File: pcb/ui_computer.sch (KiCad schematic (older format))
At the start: 0 parts

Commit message: updated power, caps, io
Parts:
- added C?: 0.1uF, RespiraWorks_Std:C_0603_1608Metric, symbol Device:C
- added C?: 1uF, RespiraWorks_Std:C_0603_1608Metric, symbol Device:C
- added H?: RaspberryPi, RespiraWorks:RaspberryPi, symbol RespiraWorks:RaspberryPi
- added J?: ESQ-120-44-L-D, RespiraWorks_Std:PinHeader_2x20_P2.54mm_Vertical, symbol RespiraWorks:ESQ-120-44-L-D
- added R? (x2): 10K, RespiraWorks_std:R_0603_1608Metric, symbol Device:R
- added R? (x2): 1K, RespiraWorks_std:R_0603_1608Metric, symbol Device:R
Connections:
- new net +3V3_Rpi: J?.1 (3V3_power), J?.17 (3V3_power), R?.1, R?.1
- new net 5V_GUI: C?.1, C?.1, J?.2 (5V_power), J?.4 (5V_power)
- new net GND: C?.2, C?.2, H?.1, J?.14 (GND), J?.20 (GND), J?.25 (GND), J?.30 (GND), J?.34 (GND), J?.39 (GND), J?.6 (GND), J?.9 (GND), R?.2, R?.2
- new net GPIO0(ID_SD): J?.27 (GPIO0(ID_SD))
- new net GPIO1(ID_SC): J?.28 (GPIO1(ID_SC))
- new net GPIO10(MOSI): J?.19 (GPIO10(MOSI))
- new net GPIO11(SCLK): J?.23 (GPIO11(SCLK))
- new net GPIO12(PWM0): J?.32 (GPIO12(PWM0))
- new net GPIO13(PWM1): J?.33 (GPIO13(PWM1))
- new net GPIO14(TXD): J?.8 (GPIO14(TXD))
- new net GPIO15(RXD): J?.10 (GPIO15(RXD))
- new net GPIO16: J?.36 (GPIO16)
- new net GPIO17: J?.11 (GPIO17)
- new net GPIO18(PCM_CLK): J?.12 (GPIO18(PCM_CLK))
- new net GPIO19(PCM_FS): J?.35 (GPIO19(PCM_FS))
- new net GPIO2(SDA): J?.3 (GPIO2(SDA))
- new net GPIO20(PCM_DIN): J?.38 (GPIO20(PCM_DIN))
- new net GPIO21(PCM_DOUT): J?.40 (GPIO21(PCM_DOUT))
- new net GPIO22: J?.15 (GPIO22)
- new net GPIO23: J?.16 (GPIO23)
- new net GPIO24: J?.18 (GPIO24)
- new net GPIO27: J?.13 (GPIO27)
- new net GPIO3(SCL): J?.5 (GPIO3(SCL))
- new net GPIO4(GPCLK0): J?.7 (GPIO4(GPCLK0))
- new net GPIO5: J?.29 (GPIO5)
- new net GPIO6: J?.31 (GPIO6)
- new net GPIO7(CE1): J?.26 (GPIO7(CE1))
- new net GPIO8(CE0): J?.24 (GPIO8(CE0))
- new net GPIO9(MISO): J?.21 (GPIO9(MISO))
- new net UI_ID0: J?.22 (GPIO25), R?.1, R?.2
- new net UI_ID1: J?.37 (GPIO26), R?.1, R?.2
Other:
- note added: "RPI powered by 5V\n"
- note added: "USB TO UART adapter: https://www.ftdichip.com/Support/Documents/DataSheets/Modules/DS_DB9-USB-RS232.pdf"

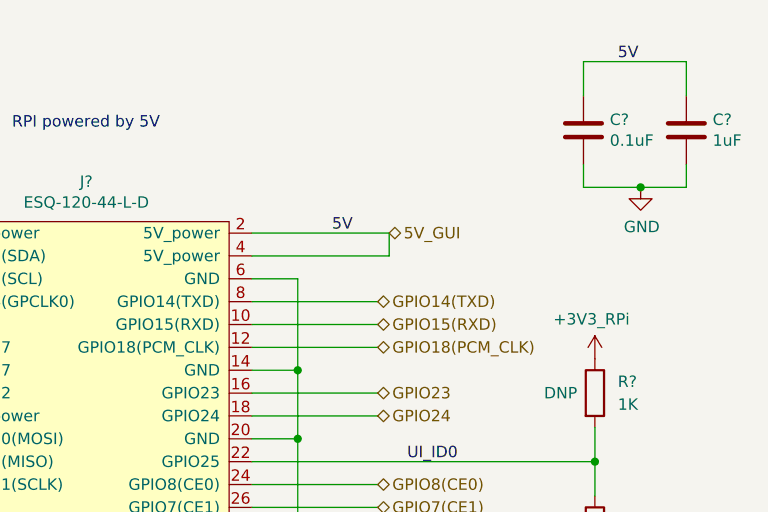
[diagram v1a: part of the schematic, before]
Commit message: Top-level beginnings, minor fixes
Started on top-level schematic blocks and connections
Started changing some net names to mixed-case-with-dash format
Fixed version number, added titles and version to all schematic sheets
Fixed incorrect SWO pin assignment in cycle controller
Added a few add'l annotations to battery sheets
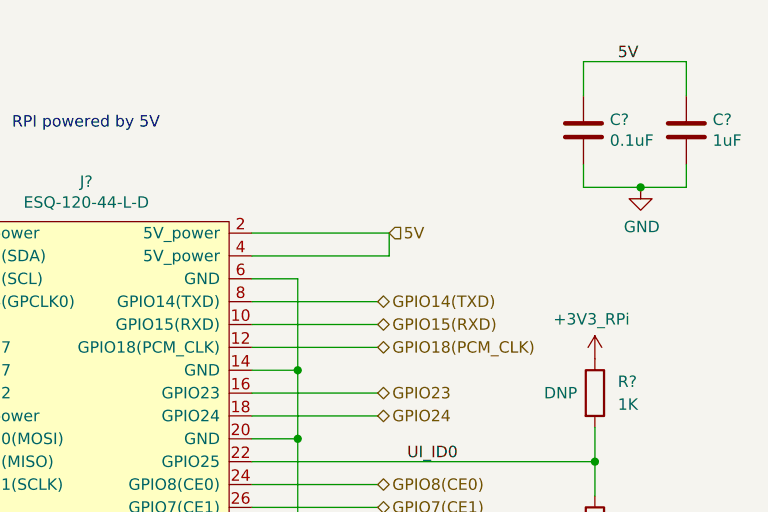
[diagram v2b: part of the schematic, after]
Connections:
- net 5V_GUI renamed 5V
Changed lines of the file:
@@
 EESchema Schematic File Version 4
-LIBS:ui_computer-cache
-EELAYER 26 0
+EELAYER 30 0
 EELAYER END
 $Descr A4 11693 8268
 encoding utf-8
-Sheet 1 1
+Sheet 8 37
 Title "UI Computer"
 Date ""
-Rev "2.0"
+Rev "A"
 Comp "RespiraWorks"
 Comment1 ""
@@
 Wire Wire Line
 	6450 4200 7000 4200
-Text HLabel 7050 2300 2    50   BiDi ~ 0
-5V_GUI
-Text Label 6800 2300 0    50   ~ 0
+Text HLabel 7050 2300 2    50   Input ~ 0
 5V
 Wire Wire Line

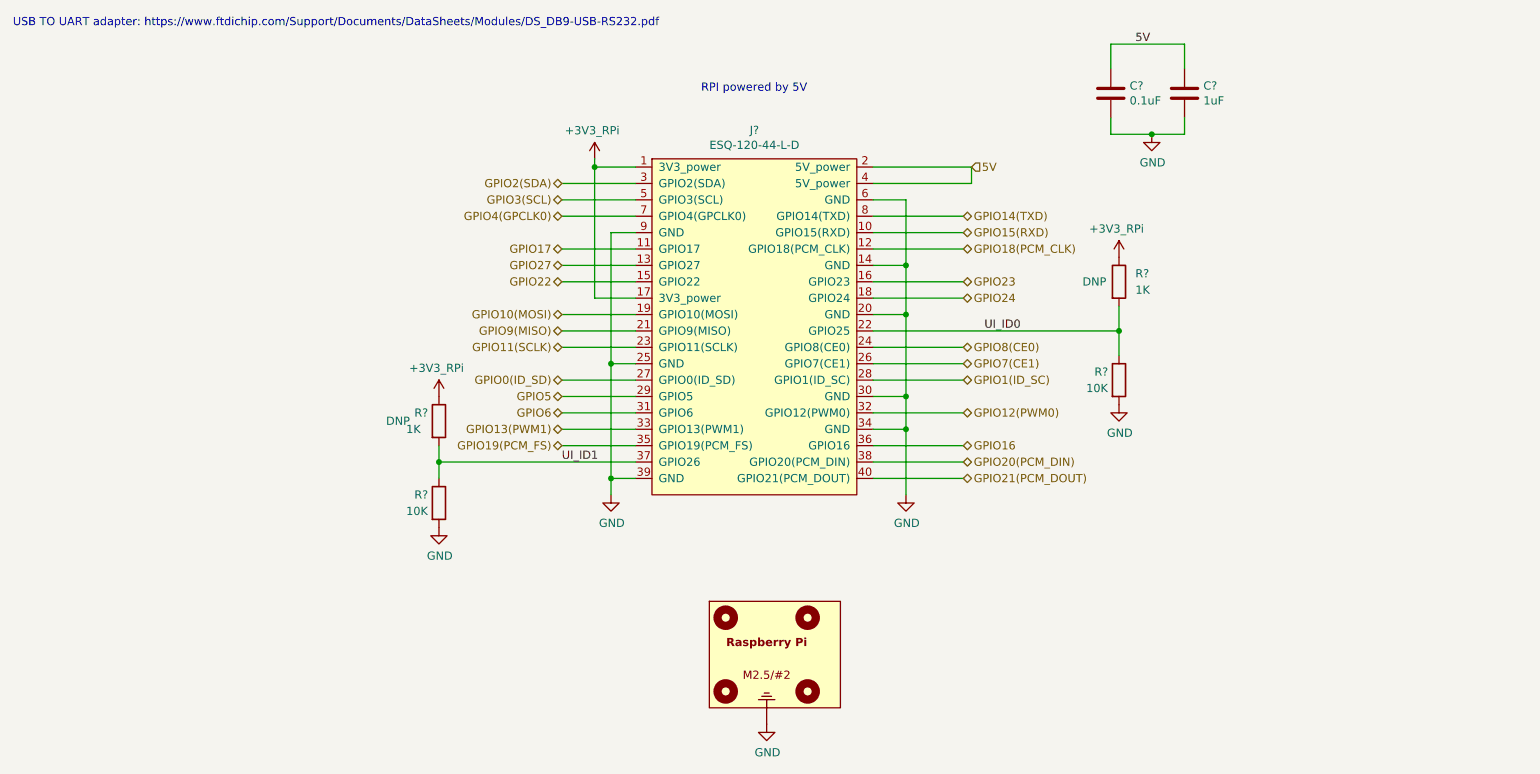
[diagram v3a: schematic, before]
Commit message: CC-I2C, BOM
Added missing pull-ups on CC-SDA, CC-SCL
First pass at BOM consolidation
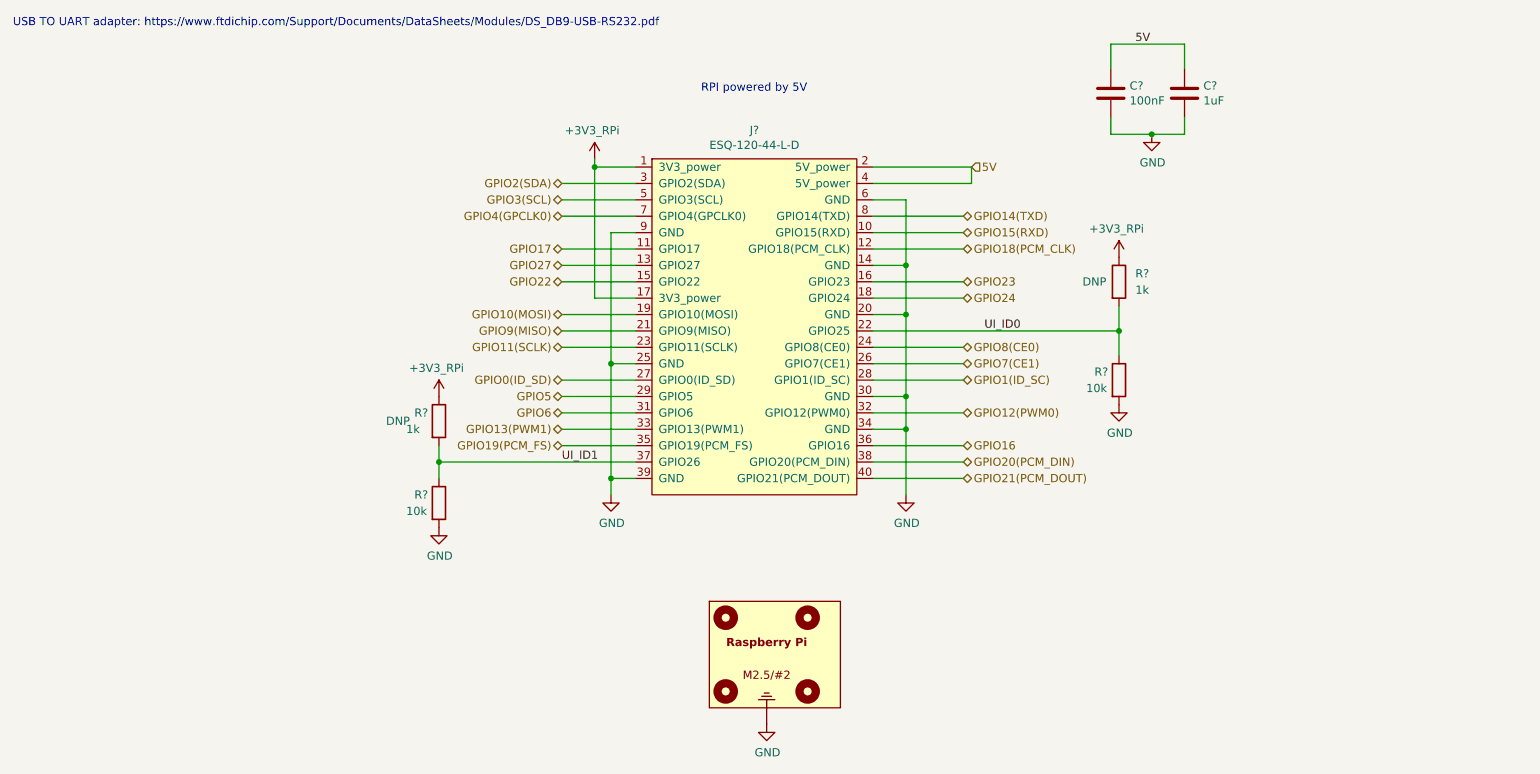
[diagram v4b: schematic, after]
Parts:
- C?: value 0.1uF -> 100nF
- R? (x2): value 10K -> 10k; footprint RespiraWorks_std:R_0603_1608Metric -> RespiraWorks_Std:R_0603_1608Metric
- R? (x2): value 1K -> 1k; footprint RespiraWorks_std:R_0603_1608Metric -> RespiraWorks_Std:R_0603_1608Metric
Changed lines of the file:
@@
 P 3800 4350
 F 0 "R?" H 3650 4400 50  0000 L CNN
-F 1 "10K" H 3600 4300 50  0000 L CNN
-F 2 "RespiraWorks_std:R_0603_1608Metric" V 3730 4350 50  0001 C CNN
+F 1 "10k" H 3600 4300 50  0000 L CNN
+F 2 "RespiraWorks_Std:R_0603_1608Metric" V 3730 4350 50  0001 C CNN
 F 3 "~" H 3800 4350 50  0001 C CNN
 	1    3800 4350
@@
 P 3800 3850
 F 0 "R?" H 3650 3900 50  0000 L CNN
-F 1 "1K" H 3600 3800 50  0000 L CNN
-F 2 "RespiraWorks_std:R_0603_1608Metric" V 3730 3850 50  0001 C CNN
+F 1 "1k" H 3600 3800 50  0000 L CNN
+F 2 "RespiraWorks_Std:R_0603_1608Metric" V 3730 3850 50  0001 C CNN
 F 3 "~" H 3800 3850 50  0001 C CNN
 F 4 "DNP" H 3550 3850 50  0000 C CNN "DNP"
@@
 P 7950 3000
 F 0 "R?" H 8050 3050 50  0000 L CNN
-F 1 "1K" H 8050 2950 50  0000 L CNN
-F 2 "RespiraWorks_std:R_0603_1608Metric" V 7880 3000 50  0001 C CNN
+F 1 "1k" H 8050 2950 50  0000 L CNN
+F 2 "RespiraWorks_Std:R_0603_1608Metric" V 7880 3000 50  0001 C CNN
 F 3 "~" H 7950 3000 50  0001 C CNN
 F 4 "DNP" H 7800 3000 50  0000 C CNN "DNP"
@@
 P 7950 3600
 F 0 "R?" H 7800 3650 50  0000 L CNN
-F 1 "10K" H 7750 3550 50  0000 L CNN
-F 2 "RespiraWorks_std:R_0603_1608Metric" V 7880 3600 50  0001 C CNN
+F 1 "10k" H 7750 3550 50  0000 L CNN
+F 2 "RespiraWorks_Std:R_0603_1608Metric" V 7880 3600 50  0001 C CNN
 F 3 "~" H 7950 3600 50  0001 C CNN
 	1    7950 3600
@@
 P 7900 1850
 F 0 "C?" H 8015 1896 50  0000 L CNN
-F 1 "0.1uF" H 8015 1805 50  0000 L CNN
+F 1 "100nF" H 8015 1805 50  0000 L CNN
 F 2 "RespiraWorks_Std:C_0603_1608Metric" H 7938 1700 50  0001 C CNN
 F 3 "~" H 7900 1850 50  0001 C CNN

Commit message: Edwin fixes
Assigned remaining footprints
Re-assigned UI computer pins to put RTS/CTS on hardware RTS/CTS, GUI-Buzzer on PWM pin
Incremented UI_ID on UI computer
Changed Oxygen-Level to Oxygen-FiO2
Removed STLink-controlled power switch on 5V-USB
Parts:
- added J?: Touchscreen power, symbol RespiraWorks_Std:Conn_01x02
- R?: value 10k -> 0
- R?: value 1k -> 0
- R?: value 1k -> 0; DNP DNP -> (none)
- R?: value 10k -> 0; DNP (none) -> DNP
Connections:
- wire segments 62 -> 63
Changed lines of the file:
@@
 P 3800 4350
 F 0 "R?" H 3650 4400 50  0000 L CNN
-F 1 "10k" H 3600 4300 50  0000 L CNN
+F 1 "0" H 3650 4300 50  0000 L CNN
 F 2 "RespiraWorks_Std:R_0603_1608Metric" V 3730 4350 50  0001 C CNN
 F 3 "~" H 3800 4350 50  0001 C CNN
@@
 P 3800 3850
 F 0 "R?" H 3650 3900 50  0000 L CNN
-F 1 "1k" H 3600 3800 50  0000 L CNN
+F 1 "0" H 3650 3800 50  0000 L CNN
 F 2 "RespiraWorks_Std:R_0603_1608Metric" V 3730 3850 50  0001 C CNN
 F 3 "~" H 3800 3850 50  0001 C CNN
@@
 P 7950 3000
 F 0 "R?" H 8050 3050 50  0000 L CNN
-F 1 "1k" H 8050 2950 50  0000 L CNN
+F 1 "0" H 8050 2950 50  0000 L CNN
 F 2 "RespiraWorks_Std:R_0603_1608Metric" V 7880 3000 50  0001 C CNN
 F 3 "~" H 7950 3000 50  0001 C CNN
-F 4 "DNP" H 7800 3000 50  0000 C CNN "DNP"
+F 4 "" H 7800 3000 50  0001 C CNN "DNP"
 	1    7950 3000
 	1    0    0    -1
@@
 U 1 1 5FE6BE04
 P 7950 3600
-F 0 "R?" H 7800 3650 50  0000 L CNN
-F 1 "10k" H 7750 3550 50  0000 L CNN
+F 0 "R?" H 8050 3650 50  0000 L CNN
+F 1 "0" H 8050 3550 50  0000 L CNN
 F 2 "RespiraWorks_Std:R_0603_1608Metric" V 7880 3600 50  0001 C CNN
 F 3 "~" H 7950 3600 50  0001 C CNN
+F 4 "DNP" H 8100 3450 50  0000 C CNN "DNP"
 	1    7950 3600
 	1    0    0    -1
@@
 Wire Wire Line
 	8150 2100 8350 2100
+$Comp
+L RespiraWorks_Std:Conn_01x02 J?
+U 1 1 60436098
+P 9850 3550
+F 0 "J?" H 9930 3542 50  0000 L CNN
+F 1 "Touchscreen power" H 9930 3451 50  0000 L CNN
+F 2 "" H 9850 3550 50  0001 C CNN
+F 3 "~" H 9850 3550 50  0001 C CNN
+	1    9850 3550
+	1    0    0    -1
+$EndComp
+Wire Wire Line
+	9650 3550 9200 3550
+Text Label 9200 3550 0    50   ~ 0
+5V
+$Comp
+L power:GND #PWR?
+U 1 1 60439316
+P 9650 3650
+F 0 "#PWR?" H 9650 3400 50  0001 C CNN
+F 1 "GND" H 9655 3477 50  0000 C CNN
+F 2 "" H 9650 3650 50  0001 C CNN
+F 3 "" H 9650 3650 50  0001 C CNN
+	1    9650 3650
+	1    0    0    -1
+$EndComp
 $EndSCHEMATC

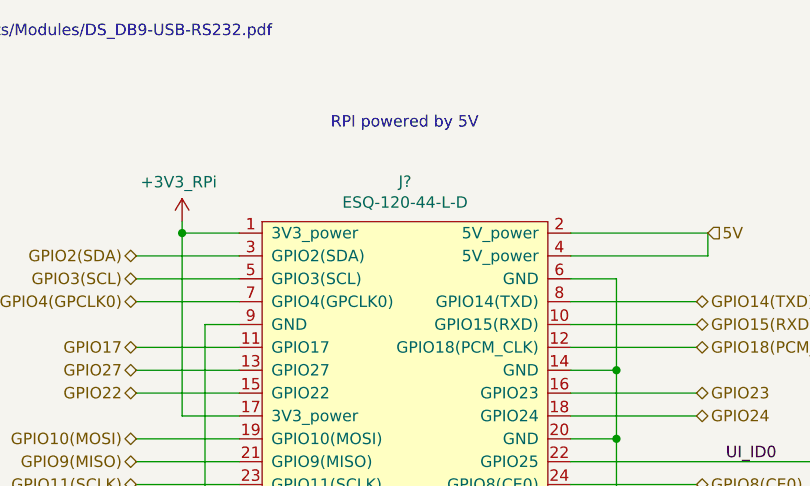
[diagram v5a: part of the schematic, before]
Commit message: BOM, fixes
Finished assigning parts, footprints except generic resistors
Added series resistors for logic signals received by UI computer to protect against UI computer power-down
Added tolerance notes on main schem
Replaced PSol fuse with PTC
Enlarged PSol driver bypass resistors to 0 ohm
Changed PSol unpopulated current-limiting resistor to divider
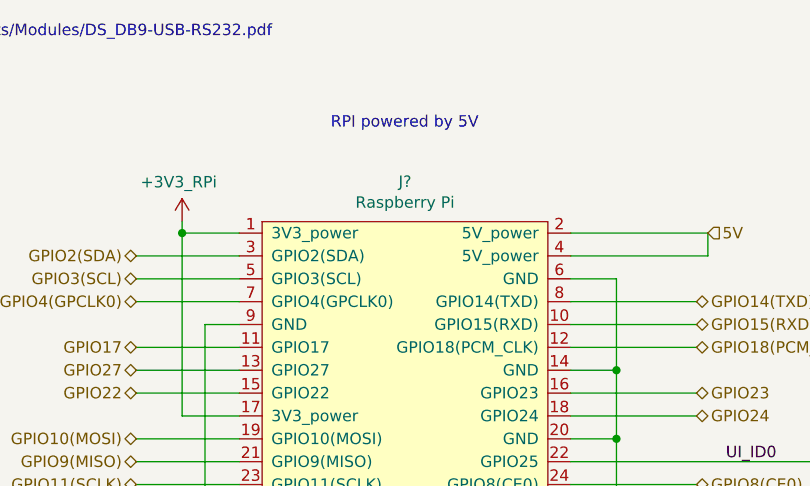
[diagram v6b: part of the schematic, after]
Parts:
- C?: Dielectric (none) -> X7R; Manufacturer (none) -> Kemet; Manufacturer PN (none) -> C0603C104K5RACTU; Voltage (none) -> 50V; Voltage Rating 10V -> (none)
- C?: Dielectric (none) -> X7R; Manufacturer (none) -> Kemet; Manufacturer PN (none) -> C0805C105K5RACTU; Voltage (none) -> 50V; Voltage Rating 10V -> (none)
- J?: value ESQ-120-44-L-D -> Raspberry Pi; Manufacturer (none) -> Samtec; Manufacturer PN (none) -> ESQ-120-44-L-D
- J?: footprint (none) -> RespiraWorks_Std:Molex_Micro-Fit_3.0_43650-0200_1x02_P3.00mm_Horizontal; Manufacturer (none) -> Molex; Manufacturer PN (none) -> 43650-0200
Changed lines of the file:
@@
 P 5700 3350
 F 0 "J?" H 5725 4625 50  0000 C CNN
-F 1 "ESQ-120-44-L-D" H 5725 4534 50  0000 C CNN
+F 1 "Raspberry Pi" H 5725 4534 50  0000 C CNN
 F 2 "RespiraWorks_Std:PinHeader_2x20_P2.54mm_Vertical" H 5100 4450 50  0001 C CNN
 F 3 "" H 5100 4450 50  0001 C CNN
+F 4 "Samtec" H 5700 3350 50  0001 C CNN "Manufacturer"
+F 5 "ESQ-120-44-L-D" H 5700 3350 50  0001 C CNN "Manufacturer PN"
 	1    5700 3350
 	1    0    0    -1
@@
 F 2 "RespiraWorks_Std:C_0603_1608Metric" H 7938 1700 50  0001 C CNN
 F 3 "~" H 7900 1850 50  0001 C CNN
-F 4 "10V" H 7900 1850 50  0001 C CNN "Voltage Rating"
+F 4 "X7R" H 7900 1850 50  0001 C CNN "Dielectric"
+F 5 "Kemet" H 7900 1850 50  0001 C CNN "Manufacturer"
+F 6 "C0603C104K5RACTU" H 7900 1850 50  0001 C CNN "Manufacturer PN"
+F 7 "50V" H 7900 1850 50  0001 C CNN "Voltage"
 	1    7900 1850
 	1    0    0    -1
@@
 F 2 "RespiraWorks_Std:C_0603_1608Metric" H 8388 1700 50  0001 C CNN
 F 3 "~" H 8350 1850 50  0001 C CNN
-F 4 "10V" H 8350 1850 50  0001 C CNN "Voltage Rating"
+F 4 "X7R" H 8350 1850 50  0001 C CNN "Dielectric"
+F 5 "Kemet" H 8350 1850 50  0001 C CNN "Manufacturer"
+F 6 "C0805C105K5RACTU" H 8350 1850 50  0001 C CNN "Manufacturer PN"
+F 7 "50V" H 8350 1850 50  0001 C CNN "Voltage"
 	1    8350 1850
 	1    0    0    -1
@@
 F 0 "J?" H 9930 3542 50  0000 L CNN
 F 1 "Touchscreen power" H 9930 3451 50  0000 L CNN
-F 2 "" H 9850 3550 50  0001 C CNN
+F 2 "RespiraWorks_Std:Molex_Micro-Fit_3.0_43650-0200_1x02_P3.00mm_Horizontal" H 9850 3550 50  0001 C CNN
 F 3 "~" H 9850 3550 50  0001 C CNN
+F 4 "Molex" H 9850 3550 50  0001 C CNN "Manufacturer"
+F 5 "43650-0200" H 9850 3550 50  0001 C CNN "Manufacturer PN"
 	1    9850 3550
 	1    0    0    -1

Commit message: Symbols
Re-assigned transistor symbols to Device:* and RespiraWorks_Std:*
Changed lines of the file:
@@
 L RespiraWorks_Std:Conn_01x02 J?
 U 1 1 60436098
-P 9850 3550
-F 0 "J?" H 9930 3542 50  0000 L CNN
-F 1 "Touchscreen power" H 9930 3451 50  0000 L CNN
-F 2 "RespiraWorks_Std:Molex_Micro-Fit_3.0_43650-0200_1x02_P3.00mm_Horizontal" H 9850 3550 50  0001 C CNN
-F 3 "~" H 9850 3550 50  0001 C CNN
-F 4 "Molex" H 9850 3550 50  0001 C CNN "Manufacturer"
-F 5 "43650-0200" H 9850 3550 50  0001 C CNN "Manufacturer PN"
-	1    9850 3550
-	1    0    0    -1
+P 9850 3650
+F 0 "J?" H 9930 3642 50  0000 L CNN
+F 1 "Touchscreen power" H 9930 3551 50  0000 L CNN
+F 2 "RespiraWorks_Std:Molex_Micro-Fit_3.0_43650-0200_1x02_P3.00mm_Horizontal" H 9850 3650 50  0001 C CNN
+F 3 "~" H 9850 3650 50  0001 C CNN
+F 4 "Molex" H 9850 3650 50  0001 C CNN "Manufacturer"
+F 5 "43650-0200" H 9850 3650 50  0001 C CNN "Manufacturer PN"
+	1    9850 3650
+	1    0    0    1
 $EndComp
 Wire Wire Line
